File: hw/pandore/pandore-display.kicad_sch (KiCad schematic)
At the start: 0 parts

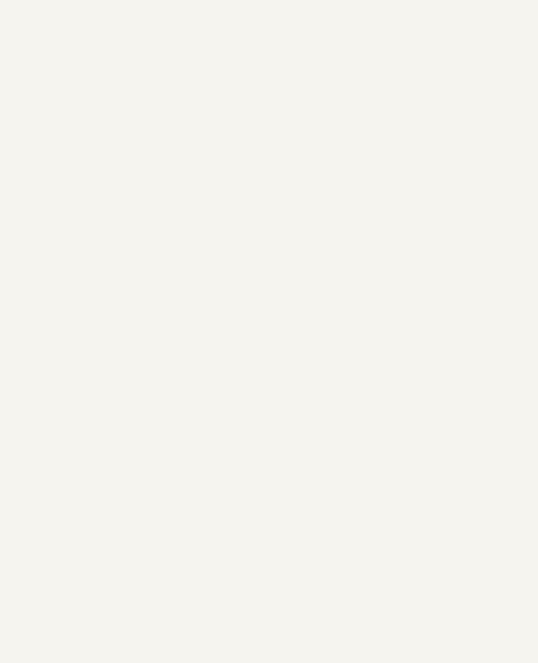
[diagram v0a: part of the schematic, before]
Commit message: added usb, hdmi and combo xlrtrs connectors resized pcb for something realistic (still wip)
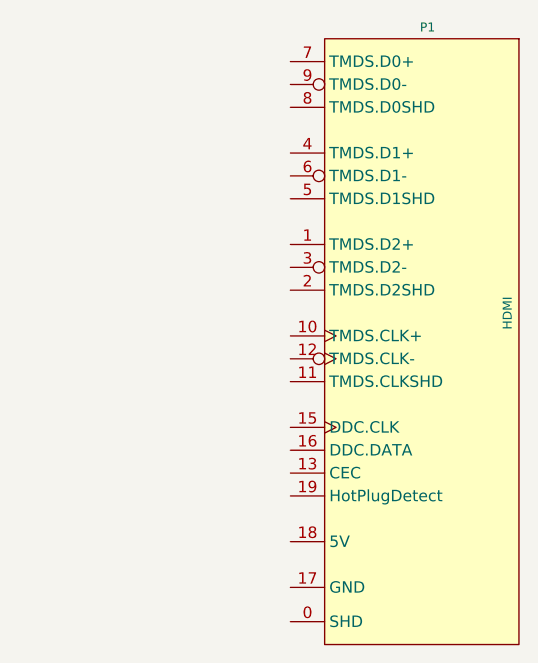
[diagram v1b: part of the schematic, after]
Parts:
- added P1: HDMI, reekilib_con:TE_1747981-1, symbol reekilib_con:HDMI
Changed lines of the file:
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@@
+		)
+	)
+	(symbol
+		(lib_id "reekilib_con:HDMI")
+		(at 224.79 90.17 0)
+		(mirror y)
+		(unit 1)
+		(exclude_from_sim no)
+		(in_bom yes)
+		(on_board yes)
+		(dnp no)
+		(fields_autoplaced yes)
+		(property "Reference" "P1"
+			(at 224.79 58.42 0)
+			(do_not_autoplace yes)
+			(effects
+				(font
+					(size 1 1)
+				)
+			)
+		)
+		(property "Value" "HDMI"
+			(at 233.68 90.17 90)
+			(do_not_autoplace yes)
+			(effects
+				(font
+					(size 1 1)
+				)
+			)
+		)
+		(property "Footprint" "reekilib_con:TE_1747981-1"
+			(at 224.79 135.255 0)
+			(do_not_autoplace yes)
+			(effects
+				(font
+					(size 1 1)
+				)
+				(hide yes)
+			)
+		)
+		(property "Datasheet" "https://www.te.com/usa-en/product-1747981-1.datasheet.pdf"
+			(at 224.79 136.525 0)
+			(do_not_autoplace yes)
+			(effects
+				(font
+					(size 1 1)
+				)
+				(hide yes)
+			)
+		)
+		(property "Description" "HDMI receptacle"
+			(at 224.79 133.985 0)
+			(do_not_autoplace yes)
+			(effects
+				(font
+					(size 1 1)
+				)
+				(hide yes)
+			)
+		)
+		(property "Vmax" "-"
+			(at 231.14 132.08 0)
+			(do_not_autoplace yes)
+			(effects
+				(font
+					(size 1 1)
+				)
+				(justify right)
+				(hide yes)
+			)
+		)
+		(property "Imax" "0.5A"
+			(at 224.79 132.08 0)
+			(do_not_autoplace yes)
+			(effects
+				(font
+					(size 1 1)
+				)
+				(hide yes)
+			)
+		)
+		(property "MPN" "1747981-1"
+			(at 224.79 128.27 0)
+			(do_not_autoplace yes)
+			(effects
+				(font
+					(size 1 1)
+				)
+				(hide yes)
+			)
+		)
+		(property "MFG" "TE connectivity"
+			(at 212.09 128.27 0)
+			(do_not_autoplace yes)
+			(effects
+				(font
+					(size 1 1)
+				)
+				(justify left)
+				(hide yes)
+			)
+		)
+		(property "Link" "https://www.te.com/usa-en/product-1747981-1.html"
+			(at 186.69 128.27 0)
+			(do_not_autoplace yes)
+			(effects
+				(font
+					(size 1 1)
+				)
+				(justify left)
+				(hide yes)
+			)
+		)
+		(pin "3"
+		)
+		(pin "9"
+		)
+		(pin "12"
+		)
+		(pin "4"
+		)
+		(pin "13"
+		)
+		(pin "0"
+		)
+		(pin "16"
+		)
+		(pin "10"
+		)
+		(pin "15"
+		)
+		(pin "11"
+		)
+		(pin "8"
+		)
+		(pin "7"
+		)
+		(pin "2"
+		)
+		(pin "18"
+		)
+		(pin "6"
+		)
+		(pin "1"
+		)
+		(pin "17"
+		)
+		(pin "19"
+		)
+		(pin "5"
+		)
+		(instances
+			(project ""
+				(path "/e55f2700-f75a-4062-8a27-fe258faa8966/db554ed3-9c74-43b8-ae28-746fed02a615"
+					(reference "P1")
+					(unit 1)
+				)
+			)
 		)
 	)

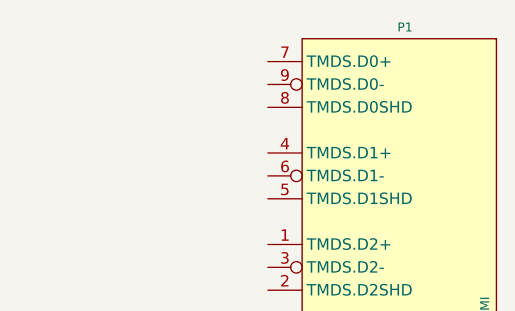
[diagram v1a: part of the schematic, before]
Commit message: added all remaining connectors (only missing M.2 now)
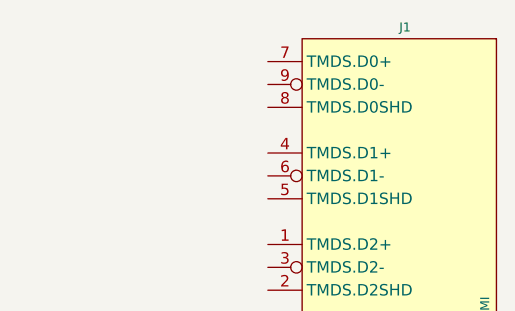
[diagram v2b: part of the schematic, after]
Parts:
- J1: renamed from P1; footprint reekilib_con:TE_1747981-1 -> reekilib_con:te_1747981-1
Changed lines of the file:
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@@
 		(dnp no)
 		(fields_autoplaced yes)
-		(property "Reference" "P1"
+		(property "Reference" "J1"
 			(at 224.79 58.42 0)
 			(do_not_autoplace yes)
@@
 			)
 		)
-		(property "Footprint" "reekilib_con:TE_1747981-1"
+		(property "Footprint" "reekilib_con:te_1747981-1"
 			(at 224.79 135.255 0)
 			(do_not_autoplace yes)
@@
 			(project ""
 				(path "/e55f2700-f75a-4062-8a27-fe258faa8966/db554ed3-9c74-43b8-ae28-746fed02a615"
-					(reference "P1")
+					(reference "J1")
 					(unit 1)
 				)

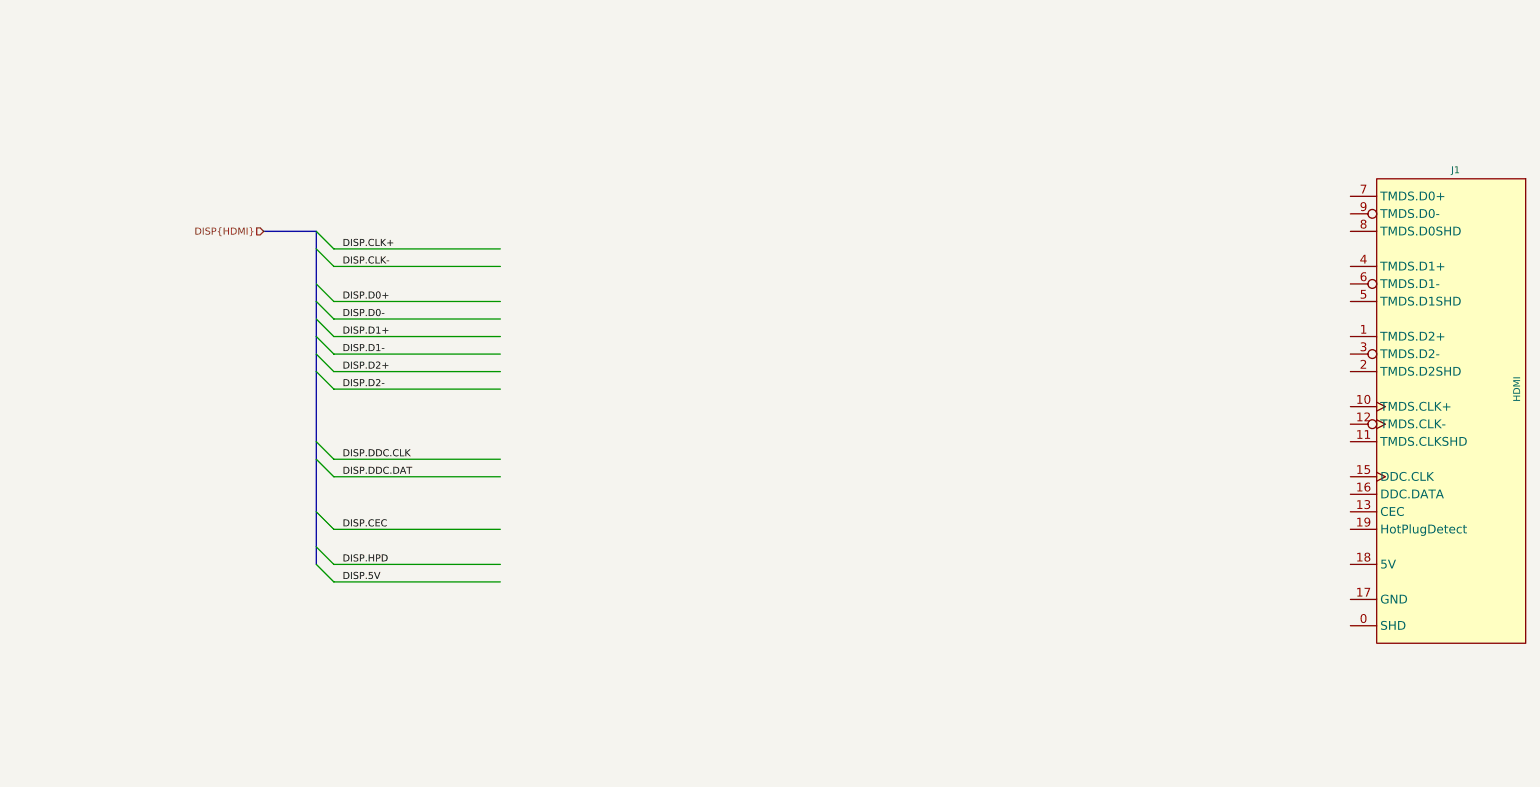
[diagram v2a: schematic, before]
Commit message: Added lots to sch and pcb: eth passive, audio codec, midi, teensy Corrected and added support for M.2
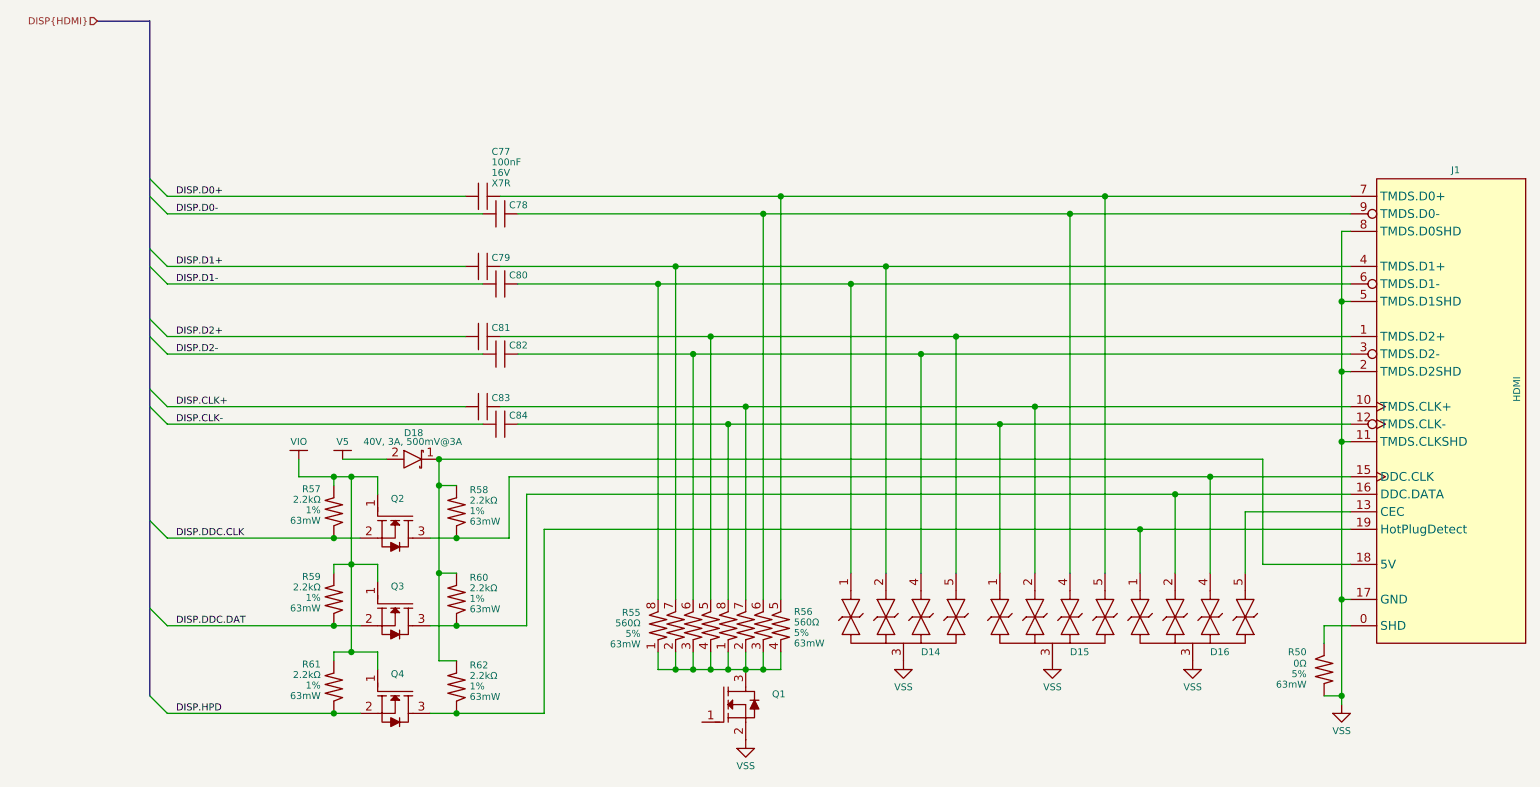
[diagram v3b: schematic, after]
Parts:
- added C77, C78, C79, C80, C81, C82, C83, C84: ${Capacitance}, ${Voltage}, ${Dielectric}, reekilib_cap:CAPC1005, symbol reekilib_cap:cap
- added D14, D15, D16: ${Vbr}, reekilib_dfn:DFN50P100X250X55-10, symbol reekilib_tvs:diode_tvsbi_4
- added D18: ${Vr}, ${Io}, ${Vf}, reekilib_dio:dio_sma, symbol reekilib_dio:diode_schottky
- added Q1, Q2, Q3, Q4: MOSFET_EN-N, reekilib_sot:SOT95P280X100-3, symbol reekilib_mfe:MOSFET_EN-N
- added R50, R57, R58, R59, R60, R61, R62: ${Resistance}, ${Tolerance}, ${Power}, reekilib_res:RESC1005, symbol reekilib_res:res
- added R55, R56: ${Resistance}, ${Tolerance}, ${Power}, reekilib_res:RESCAXSR50P200X100X35-8, symbol reekilib_res:res_4
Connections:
- net DISP.CLK+: now also C83.2
- net DISP.CLK-: now also C84.2
- net DISP.D0+: now also C77.2
- net DISP.D0-: now also C78.2
- net DISP.D1+: now also C79.2
- net DISP.D1-: now also C80.2
- net DISP.D2+: now also C81.2
- net DISP.D2-: now also C82.2
- net DISP.DDC.CLK: now also Q2.2 (S), R57.2
- net DISP.DDC.DAT: now also Q3.2 (S), R59.2
- net DISP.HPD: now also Q4.2 (S), R61.2
- net at J1.0 (SHD): now also R50.2
- net at J1.1 (TMDS.D2+): now also C81.1, D14.5, R55.5
- net at J1.10 (TMDS.CLK+): now also C83.1, D15.2, R56.7
- net VSS: now reaches J1.11 (TMDS.CLKSHD)
- net VSS: now also J1.17 (GND), J1.2 (TMDS.D2SHD), J1.5 (TMDS.D1SHD), J1.8 (TMDS.D0SHD), D14.3, D15.3, D16.3, Q1.2 (S), R50.1
- net at J1.12 (TMDS.CLK-): now also C84.1, D15.1, R56.8
- net at J1.13 (CEC): now also D16.5
- net at J1.15 (DDC.CLK): now also D16.4, Q2.3 (D), R58.2
- net at J1.16 (DDC.DATA): now also D16.2, Q3.3 (D), R60.2
- net at J1.18 (5V): now also D18.1 (C), R58.1, R60.1, R62.1
- net at J1.19 (HotPlugDetect): now also D16.1, Q4.3 (D), R62.2
- net at J1.3 (TMDS.D2-): now also C82.1, D14.4, R55.6
- net at J1.4 (TMDS.D1+): now also C79.1, D14.2, R55.7
- net at J1.6 (TMDS.D1-): now also C80.1, D14.1, R55.8
- net at J1.7 (TMDS.D0+): now also C77.1, D15.5, R56.5
- net at J1.9 (TMDS.D0-): now also C78.1, D15.4, R56.6
- new net: Q1.3 (D), R55.1, R55.2, R55.3, R55.4, R56.1, R56.2, R56.3, R56.4
- new net V5: D18.2 (A)
- new net VIO: Q2.1 (G), Q3.1 (G), Q4.1 (G), R57.1, R59.1, R61.1

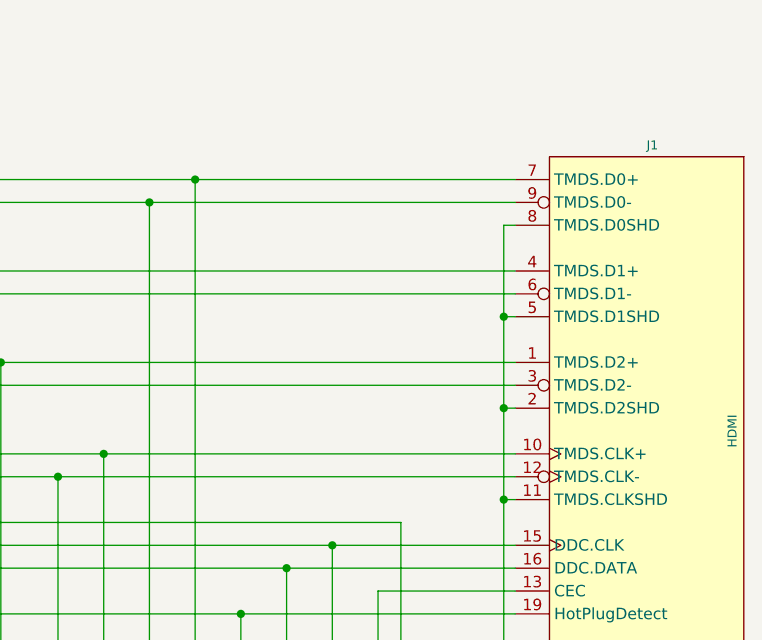
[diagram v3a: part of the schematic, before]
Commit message: Lots of routing done power blocks intra-routing mostly done rp2350 routing mostly done some label cleanup
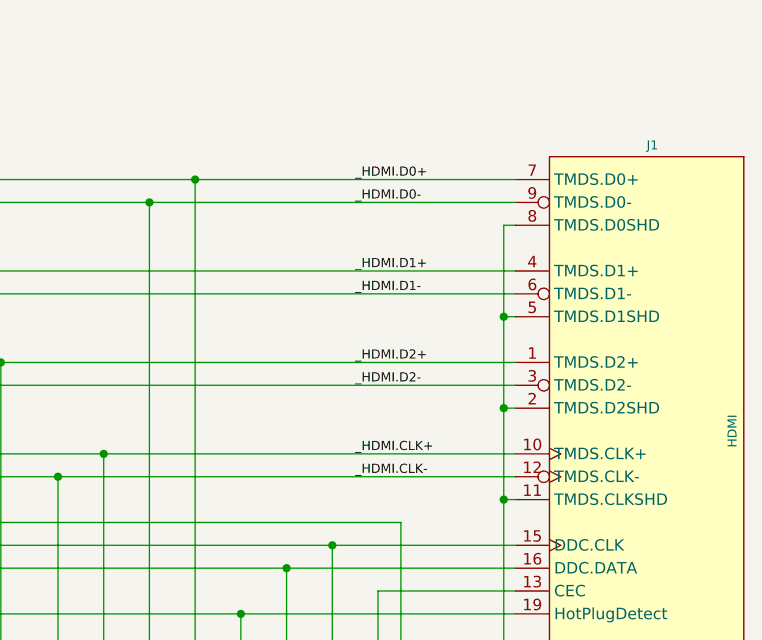
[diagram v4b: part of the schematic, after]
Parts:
- D14, D15, D16: footprint reekilib_dfn:DFN50P100X250X55-10 -> reekilib_dfn:DFN50P100X250X55-10_ESD204
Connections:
- net _HDMI.D1-: now reaches C80.1, D14.1, J1.6 (TMDS.D1-), R55.8
- net _HDMI.D1+: now reaches C79.1, D14.2, J1.4 (TMDS.D1+), R55.7
- net _HDMI.D2-: now reaches C82.1, D14.4, J1.3 (TMDS.D2-), R55.6
- net _HDMI.D2+: now reaches C81.1, D14.5, J1.1 (TMDS.D2+), R55.5
- net _HDMI.D0-: now reaches C78.1, D15.4, J1.9 (TMDS.D0-), R56.6
- net _HDMI.CLK-: now reaches C84.1, D15.1, J1.12 (TMDS.CLK-), R56.8
- net _HDMI.CLK+: now reaches C83.1, D15.2, J1.10 (TMDS.CLK+), R56.7
- net _HDMI.D0+: now reaches C77.1, D15.5, J1.7 (TMDS.D0+), R56.5
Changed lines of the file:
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@@
 		)
 	)
+	(label "_HDMI.CLK+"
+		(at 191.77 92.71 0)
+		(effects
+			(font
+				(size 1.016 1.016)
+			)
+			(justify left bottom)
+		)
+	)
 	(label "DISP.D2+"
 		(at 39.37 82.55 0)
@@
 		)
 	)
+	(label "_HDMI.CLK-"
+		(at 191.77 95.25 0)
+		(effects
+			(font
+				(size 1.016 1.016)
+			)
+			(justify left bottom)
+		)
+	)
+	(label "_HDMI.D1-"
+		(at 191.77 74.93 0)
+		(effects
+			(font
+				(size 1.016 1.016)
+			)
+			(justify left bottom)
+		)
+	)
+	(label "_HDMI.D0+"
+		(at 191.77 62.23 0)
+		(effects
+			(font
+				(size 1.016 1.016)
+			)
+			(justify left bottom)
+		)
+	)
+	(label "_HDMI.D1+"
+		(at 191.77 72.39 0)
+		(effects
+			(font
+				(size 1.016 1.016)
+			)
+			(justify left bottom)
+		)
+	)
+	(label "_HDMI.D2-"
+		(at 191.77 85.09 0)
+		(effects
+			(font
+				(size 1.016 1.016)
+			)
+			(justify left bottom)
+		)
+	)
+	(label "_HDMI.D0-"
+		(at 191.77 64.77 0)
+		(effects
+			(font
+				(size 1.016 1.016)
+			)
+			(justify left bottom)
+		)
+	)
 	(label "DISP.DDC.CLK"
 		(at 39.37 111.76 0)
@@
 		)
 	)
+	(label "_HDMI.D2+"
+		(at 191.77 82.55 0)
+		(effects
+			(font
+				(size 1.016 1.016)
+			)
+			(justify left bottom)
+		)
+	)
 	(hierarchical_label "DISP{HDMI}"
 		(shape input)
@@
 			)
 		)
-		(property "Footprint" "reekilib_dfn:DFN50P100X250X55-10"
+		(property "Footprint" "reekilib_dfn:DFN50P100X250X55-10_ESD204"
 			(at 186.69 139.7 0)
 			(do_not_autoplace yes)
@@
 			)
 		)
-		(property "Footprint" "reekilib_dfn:DFN50P100X250X55-10"
+		(property "Footprint" "reekilib_dfn:DFN50P100X250X55-10_ESD204"
 			(at 144.78 139.7 0)
 			(do_not_autoplace yes)
@@
 			)
 		)
-		(property "Footprint" "reekilib_dfn:DFN50P100X250X55-10"
+		(property "Footprint" "reekilib_dfn:DFN50P100X250X55-10_ESD204"
 			(at 166.37 139.7 0)
 			(do_not_autoplace yes)

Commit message: added todos following review
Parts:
- R55, R56: now not fitted
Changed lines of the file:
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@@
 		(in_bom yes)
 		(on_board yes)
-		(dnp no)
+		(dnp yes)
 		(property "Reference" "R56"
 			(at 128.905 122.428 0)
@@
 		(in_bom yes)
 		(on_board yes)
-		(dnp no)
+		(dnp yes)
 		(property "Reference" "R55"
 			(at 106.68 122.555 0)
